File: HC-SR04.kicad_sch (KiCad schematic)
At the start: 3 parts, among them J5 Conn_01x04_Pin

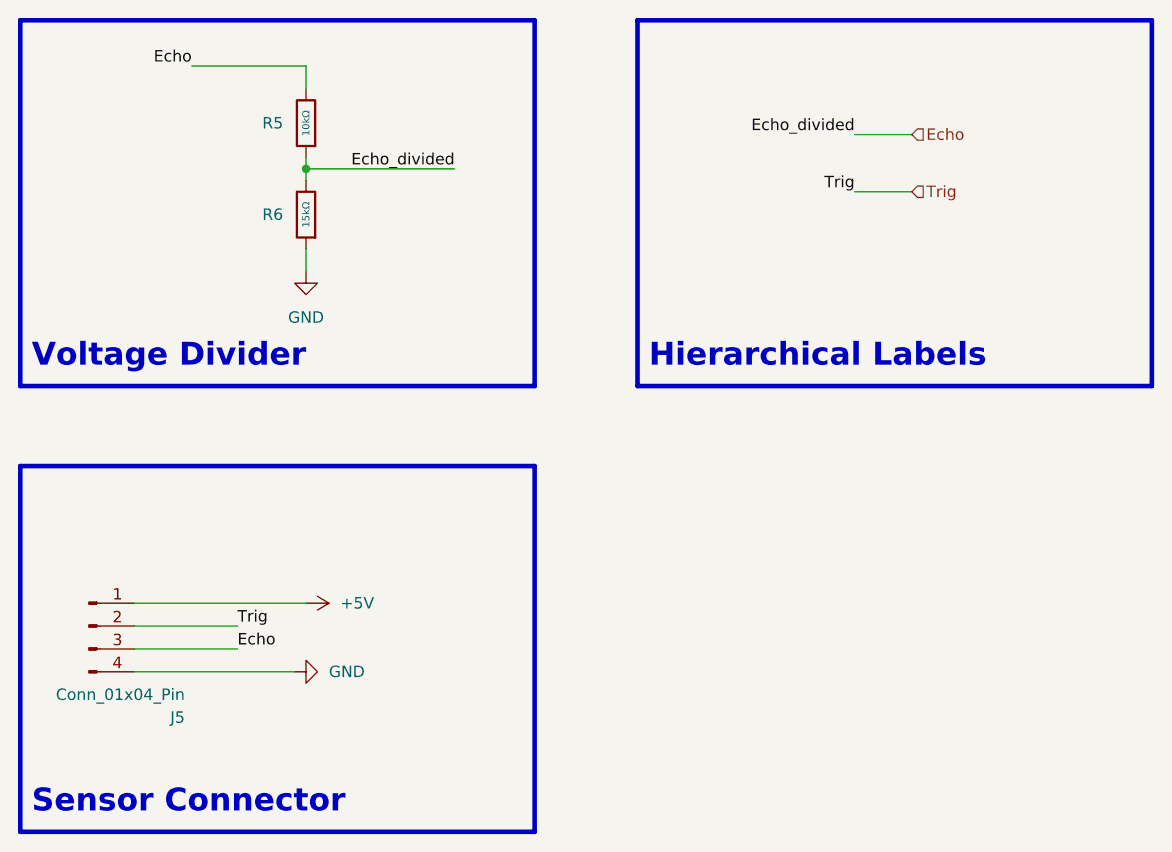
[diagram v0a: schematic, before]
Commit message: finished routing and exported gerber
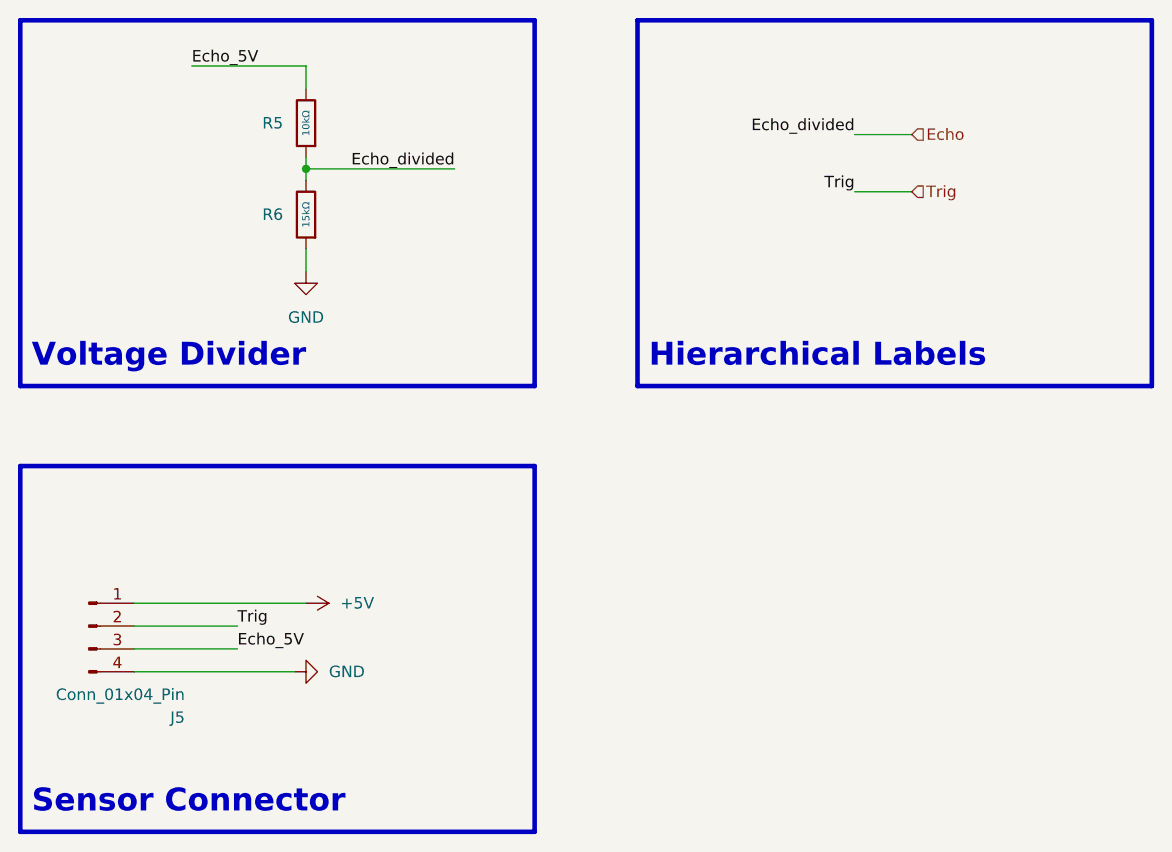
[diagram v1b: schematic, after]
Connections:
- net Echo: no longer J5.3 (Pin_3), R5.2
- new net Echo_5V: J5.3 (Pin_3), R5.2
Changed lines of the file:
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@@
 		)
 	)
-	(label "Echo"
-		(at 99.06 60.96 180)
+	(label "Echo_5V"
+		(at 99.06 60.96 0)
 		(effects
 			(font
 				(size 1.27 1.27)
 			)
-			(justify right bottom)
+			(justify left bottom)
 		)
 	)
@@
 		)
 	)
-	(label "Echo"
+	(label "Echo_5V"
 		(at 104.14 125.73 0)
 		(effects
